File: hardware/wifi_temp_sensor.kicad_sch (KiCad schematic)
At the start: 12 parts, among them J1 USB_B_Mini, J2 ESP8266, J3 TempSensor, J4 Prog, J5 Aux_I2C, SW1 BootMode, U2 AZ1117-3.3

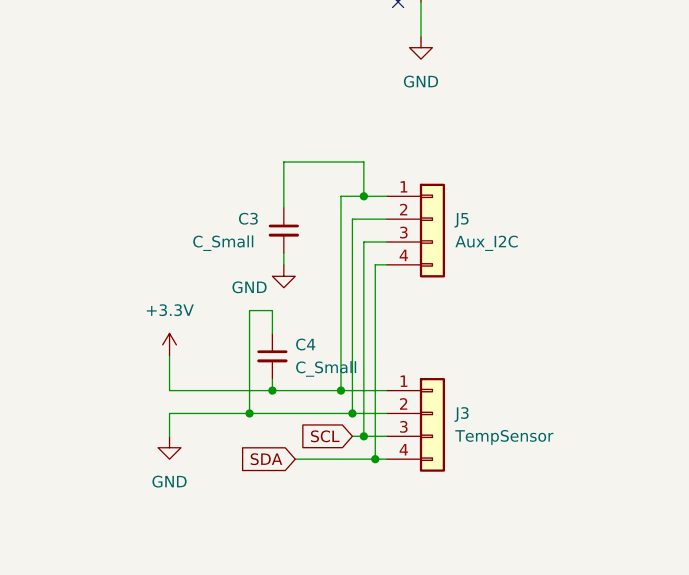
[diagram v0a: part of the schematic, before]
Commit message: minor change to fit OLED screen connector
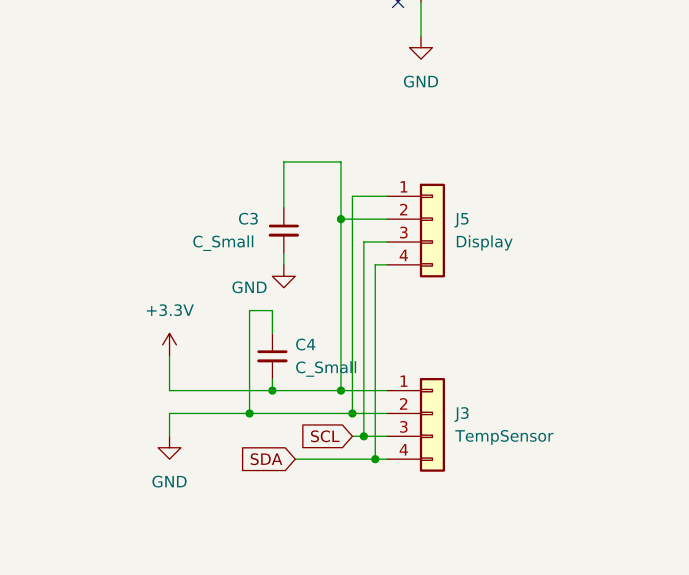
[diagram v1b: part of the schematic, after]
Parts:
- J5: value Aux_I2C -> Display
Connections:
- net +3.3V: now also J5.2 (Pin_2); no longer J5.1 (Pin_1)
- net GND: now also J5.1 (Pin_1); no longer J5.2 (Pin_2)
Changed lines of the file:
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@@
   (junction (at 177.8 40.64) (diameter 0) (color 0 0 0 0)
   )
+  (junction (at 241.3 113.03) (diameter 0) (color 0 0 0 0)
+  )
+  (junction (at 237.49 86.36) (diameter 0) (color 0 0 0 0)
+  )
+  (junction (at 163.83 53.34) (diameter 0) (color 0 0 0 0)
+  )
+  (junction (at 229.87 105.41) (diameter 0) (color 0 0 0 0)
+  )
+  (junction (at 227.33 107.95) (diameter 0) (color 0 0 0 0)
+  )
+  (junction (at 240.03 110.49) (diameter 0) (color 0 0 0 0)
+  )
+  (junction (at 238.76 107.95) (diameter 0) (color 0 0 0 0)
+  )
   (junction (at 237.49 105.41) (diameter 0) (color 0 0 0 0)
   )
-  (junction (at 241.3 113.03) (diameter 0) (color 0 0 0 0)
-  )
-  (junction (at 240.03 83.82) (diameter 0) (color 0 0 0 0)
-  )
-  (junction (at 163.83 53.34) (diameter 0) (color 0 0 0 0)
-  )
-  (junction (at 229.87 105.41) (diameter 0) (color 0 0 0 0)
-  )
-  (junction (at 227.33 107.95) (diameter 0) (color 0 0 0 0)
-  )
-  (junction (at 240.03 110.49) (diameter 0) (color 0 0 0 0)
-  )
   (junction (at 148.59 40.64) (diameter 0) (color 0 0 0 0)
   )
   (junction (at 176.53 114.3) (diameter 0) (color 0 0 0 0)
-  )
-  (junction (at 238.76 107.95) (diameter 0) (color 0 0 0 0)
   )
   (no_connect (at 254 52.07))
@@
   (no_connect (at 242.57 157.48))
   (no_connect (at 242.57 147.32))
-  (wire (pts (xy 242.57 105.41) (xy 237.49 105.41))
+  (wire (pts (xy 229.87 105.41) (xy 237.49 105.41))
     (stroke (width 0) (type default))
   )
@@
     (stroke (width 0) (type default))
   )
+  (wire (pts (xy 237.49 86.36) (xy 237.49 105.41))
+    (stroke (width 0) (type default))
+  )
+  (wire (pts (xy 237.49 105.41) (xy 242.57 105.41))
+    (stroke (width 0) (type default))
+  )
   (wire (pts (xy 148.59 53.34) (xy 163.83 53.34))
     (stroke (width 0) (type default))
@@
     (stroke (width 0) (type default))
   )
+  (wire (pts (xy 242.57 86.36) (xy 237.49 86.36))
+    (stroke (width 0) (type default))
+  )
   (wire (pts (xy 234.95 138.43) (xy 234.95 149.86))
     (stroke (width 0) (type default))
@@
     (stroke (width 0) (type default))
   )
-  (wire (pts (xy 237.49 105.41) (xy 229.87 105.41))
+  (wire (pts (xy 240.03 88.9) (xy 242.57 88.9))
+    (stroke (width 0) (type default))
+  )
+  (wire (pts (xy 229.87 99.06) (xy 229.87 96.52))
+    (stroke (width 0) (type default))
+  )
+  (wire (pts (xy 176.53 114.3) (xy 194.31 114.3))
+    (stroke (width 0) (type default))
+  )
+  (wire (pts (xy 231.14 80.01) (xy 237.49 80.01))
+    (stroke (width 0) (type default))
+  )
+  (wire (pts (xy 231.14 90.17) (xy 231.14 91.44))
+    (stroke (width 0) (type default))
+  )
+  (wire (pts (xy 222.25 154.94) (xy 242.57 154.94))
+    (stroke (width 0) (type default))
+  )
+  (wire (pts (xy 175.26 153.67) (xy 179.07 153.67))
+    (stroke (width 0) (type default))
+  )
+  (wire (pts (xy 232.41 152.4) (xy 242.57 152.4))
+    (stroke (width 0) (type default))
+  )
+  (wire (pts (xy 229.87 96.52) (xy 227.33 96.52))
+    (stroke (width 0) (type default))
+  )
+  (wire (pts (xy 143.51 40.64) (xy 148.59 40.64))
+    (stroke (width 0) (type default))
+  )
+  (wire (pts (xy 238.76 144.78) (xy 238.76 146.05))
+    (stroke (width 0) (type default))
+  )
+  (wire (pts (xy 259.08 46.99) (xy 254 46.99))
+    (stroke (width 0) (type default))
+  )
+  (wire (pts (xy 153.67 121.92) (xy 153.67 124.46))
+    (stroke (width 0) (type default))
+  )
+  (wire (pts (xy 259.08 44.45) (xy 259.08 46.99))
+    (stroke (width 0) (type default))
+  )
+  (wire (pts (xy 176.53 114.3) (xy 176.53 111.76))
+    (stroke (width 0) (type default))
+  )
+  (wire (pts (xy 163.83 48.26) (xy 163.83 53.34))
+    (stroke (width 0) (type default))
+  )
+  (wire (pts (xy 241.3 91.44) (xy 242.57 91.44))
+    (stroke (width 0) (type default))
+  )
+  (wire (pts (xy 179.07 153.67) (xy 179.07 156.21))
+    (stroke (width 0) (type default))
+  )
+  (wire (pts (xy 241.3 91.44) (xy 241.3 113.03))
+    (stroke (width 0) (type default))
+  )
+  (wire (pts (xy 163.83 53.34) (xy 177.8 53.34))
+    (stroke (width 0) (type default))
+  )
+  (wire (pts (xy 177.8 48.26) (xy 177.8 53.34))
     (stroke (width 0) (type default))
   )
@@
     (stroke (width 0) (type default))
   )
-  (wire (pts (xy 240.03 88.9) (xy 242.57 88.9))
-    (stroke (width 0) (type default))
-  )
-  (wire (pts (xy 240.03 83.82) (xy 242.57 83.82))
-    (stroke (width 0) (type default))
-  )
-  (wire (pts (xy 229.87 99.06) (xy 229.87 96.52))
-    (stroke (width 0) (type default))
-  )
-  (wire (pts (xy 176.53 114.3) (xy 194.31 114.3))
-    (stroke (width 0) (type default))
-  )
-  (wire (pts (xy 231.14 90.17) (xy 231.14 91.44))
-    (stroke (width 0) (type default))
-  )
-  (wire (pts (xy 231.14 80.01) (xy 240.03 80.01))
-    (stroke (width 0) (type default))
-  )
-  (wire (pts (xy 237.49 105.41) (xy 237.49 83.82))
-    (stroke (width 0) (type default))
-  )
-  (wire (pts (xy 222.25 154.94) (xy 242.57 154.94))
-    (stroke (width 0) (type default))
-  )
-  (wire (pts (xy 175.26 153.67) (xy 179.07 153.67))
-    (stroke (width 0) (type default))
-  )
-  (wire (pts (xy 232.41 152.4) (xy 242.57 152.4))
-    (stroke (width 0) (type default))
-  )
-  (wire (pts (xy 229.87 96.52) (xy 227.33 96.52))
-    (stroke (width 0) (type default))
-  )
-  (wire (pts (xy 143.51 40.64) (xy 148.59 40.64))
-    (stroke (width 0) (type default))
-  )
-  (wire (pts (xy 238.76 144.78) (xy 238.76 146.05))
-    (stroke (width 0) (type default))
-  )
-  (wire (pts (xy 259.08 46.99) (xy 254 46.99))
-    (stroke (width 0) (type default))
-  )
-  (wire (pts (xy 153.67 121.92) (xy 153.67 124.46))
-    (stroke (width 0) (type default))
-  )
-  (wire (pts (xy 259.08 44.45) (xy 259.08 46.99))
-    (stroke (width 0) (type default))
-  )
-  (wire (pts (xy 176.53 114.3) (xy 176.53 111.76))
-    (stroke (width 0) (type default))
-  )
-  (wire (pts (xy 163.83 48.26) (xy 163.83 53.34))
-    (stroke (width 0) (type default))
-  )
-  (wire (pts (xy 241.3 91.44) (xy 242.57 91.44))
-    (stroke (width 0) (type default))
-  )
-  (wire (pts (xy 179.07 153.67) (xy 179.07 156.21))
-    (stroke (width 0) (type default))
-  )
-  (wire (pts (xy 240.03 80.01) (xy 240.03 83.82))
-    (stroke (width 0) (type default))
-  )
-  (wire (pts (xy 241.3 91.44) (xy 241.3 113.03))
-    (stroke (width 0) (type default))
-  )
-  (wire (pts (xy 163.83 53.34) (xy 177.8 53.34))
-    (stroke (width 0) (type default))
-  )
-  (wire (pts (xy 177.8 48.26) (xy 177.8 53.34))
-    (stroke (width 0) (type default))
-  )
   (wire (pts (xy 148.59 40.64) (xy 148.59 43.18))
     (stroke (width 0) (type default))
   )
-  (wire (pts (xy 237.49 83.82) (xy 240.03 83.82))
+  (wire (pts (xy 238.76 83.82) (xy 238.76 107.95))
     (stroke (width 0) (type default))
   )
@@
     (stroke (width 0) (type default))
   )
-  (wire (pts (xy 238.76 107.95) (xy 238.76 86.36))
-    (stroke (width 0) (type default))
-  )
   (wire (pts (xy 173.99 121.92) (xy 180.34 121.92))
     (stroke (width 0) (type default))
   )
-  (wire (pts (xy 238.76 86.36) (xy 242.57 86.36))
-    (stroke (width 0) (type default))
-  )
   (wire (pts (xy 218.44 105.41) (xy 218.44 101.6))
     (stroke (width 0) (type default))
@@
     (stroke (width 0) (type default))
   )
+  (wire (pts (xy 242.57 83.82) (xy 238.76 83.82))
+    (stroke (width 0) (type default))
+  )
   (wire (pts (xy 241.3 113.03) (xy 242.57 113.03))
+    (stroke (width 0) (type default))
+  )
+  (wire (pts (xy 237.49 80.01) (xy 237.49 86.36))
     (stroke (width 0) (type default))
   )
@@
       (effects (font (size 1.27 1.27)) (justify left))
     )
-    (property "Value" "Aux_I2C" (at 250.19 88.9 0)
+    (property "Value" "Display" (at 250.19 88.9 0)
       (effects (font (size 1.27 1.27)) (justify left))
     )

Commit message: Minor tweaks
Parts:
- J4: footprint Connector_PinHeader_2.54mm:PinHeader_1x06_P2.54mm_Vertical -> Connector_PinSocket_2.54mm:PinSocket_1x06_P2.54mm_Horizontal
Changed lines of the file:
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@@
       (effects (font (size 1.27 1.27)) (justify left))
     )
-    (property "Footprint" "Connector_PinHeader_2.54mm:PinHeader_1x06_P2.54mm_Vertical" (at 247.65 149.86 0)
+    (property "Footprint" "Connector_PinSocket_2.54mm:PinSocket_1x06_P2.54mm_Horizontal" (at 247.65 149.86 0)
       (effects (font (size 1.27 1.27)) hide)
     )

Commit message: Final mods for V0.3, added right angle switch
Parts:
- C1, C2, C3, C4, C5: footprint Capacitor_SMD:C_1206_3216Metric -> Capacitor_SMD:C_1206_3216Metric_Pad1.33x1.80mm_HandSolder
- SW1: footprint Button_Switch_THT:SW_PUSH_6mm -> buttons:TL1105RA
- U2: footprint Package_TO_SOT_SMD:SOT-89-3 -> Package_TO_SOT_SMD:SOT-89-3_Handsoldering
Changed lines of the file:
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@@
       (effects (font (size 1.27 1.27)))
     )
-    (property "Footprint" "Button_Switch_THT:SW_PUSH_6mm" (at 167.64 153.67 0)
+    (property "Footprint" "buttons:TL1105RA" (at 167.64 153.67 0)
       (effects (font (size 1.27 1.27)) hide)
     )
@@
       (effects (font (size 1.27 1.27)) (justify left))
     )
-    (property "Footprint" "Capacitor_SMD:C_1206_3216Metric" (at 231.14 87.63 0)
+    (property "Footprint" "Capacitor_SMD:C_1206_3216Metric_Pad1.33x1.80mm_HandSolder" (at 231.14 87.63 0)
       (effects (font (size 1.27 1.27)) hide)
     )
@@
       (effects (font (size 1.27 1.27)) (justify left))
     )
-    (property "Footprint" "Capacitor_SMD:C_1206_3216Metric" (at 229.87 101.6 0)
+    (property "Footprint" "Capacitor_SMD:C_1206_3216Metric_Pad1.33x1.80mm_HandSolder" (at 229.87 101.6 0)
       (effects (font (size 1.27 1.27)) hide)
     )
@@
       (effects (font (size 1.27 1.27)) (justify left))
     )
-    (property "Footprint" "Capacitor_SMD:C_1206_3216Metric" (at 148.59 45.72 0)
+    (property "Footprint" "Capacitor_SMD:C_1206_3216Metric_Pad1.33x1.80mm_HandSolder" (at 148.59 45.72 0)
       (effects (font (size 1.27 1.27)) hide)
     )
@@
       (effects (font (size 1.27 1.27)) (justify left))
     )
-    (property "Footprint" "Capacitor_SMD:C_1206_3216Metric" (at 177.8 45.72 0)
+    (property "Footprint" "Capacitor_SMD:C_1206_3216Metric_Pad1.33x1.80mm_HandSolder" (at 177.8 45.72 0)
       (effects (font (size 1.27 1.27)) hide)
     )
@@
       (effects (font (size 1.27 1.27)) (justify left))
     )
-    (property "Footprint" "Capacitor_SMD:C_1206_3216Metric" (at 194.31 116.84 0)
+    (property "Footprint" "Capacitor_SMD:C_1206_3216Metric_Pad1.33x1.80mm_HandSolder" (at 194.31 116.84 0)
       (effects (font (size 1.27 1.27)) hide)
     )
@@
       (effects (font (size 1.27 1.27)))
     )
-    (property "Footprint" "Package_TO_SOT_SMD:SOT-89-3" (at 163.83 34.29 0)
+    (property "Footprint" "Package_TO_SOT_SMD:SOT-89-3_Handsoldering" (at 163.83 34.29 0)
       (effects (font (size 1.27 1.27) italic) hide)
     )
